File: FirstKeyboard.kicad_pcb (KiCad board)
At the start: 2 copper layers, 32 parts, among them SW1 SW_Push, U1 ATmega32U4-AU, Y1 16MHz

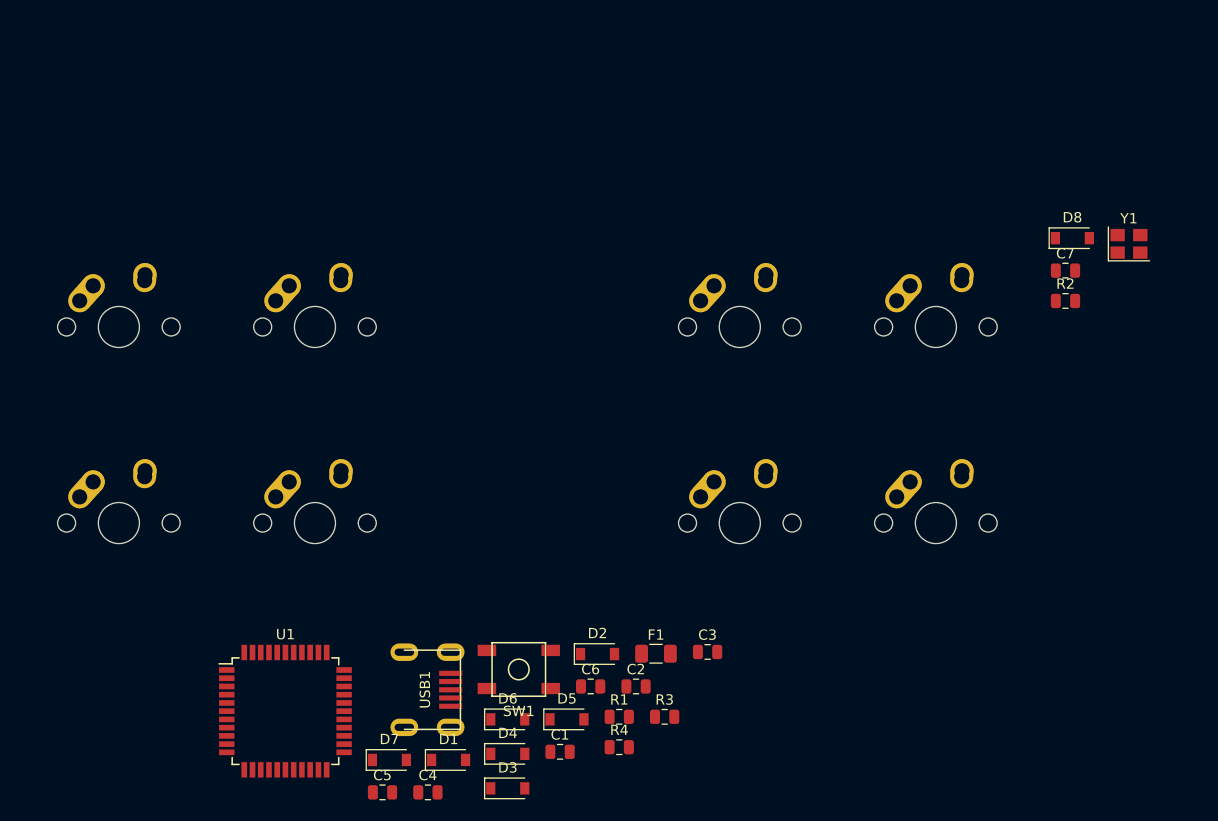
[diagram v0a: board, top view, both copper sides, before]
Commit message: Readjusted switch footprints to desired spacing of later project. Moved diodes on bottom side, within switch footprint area.
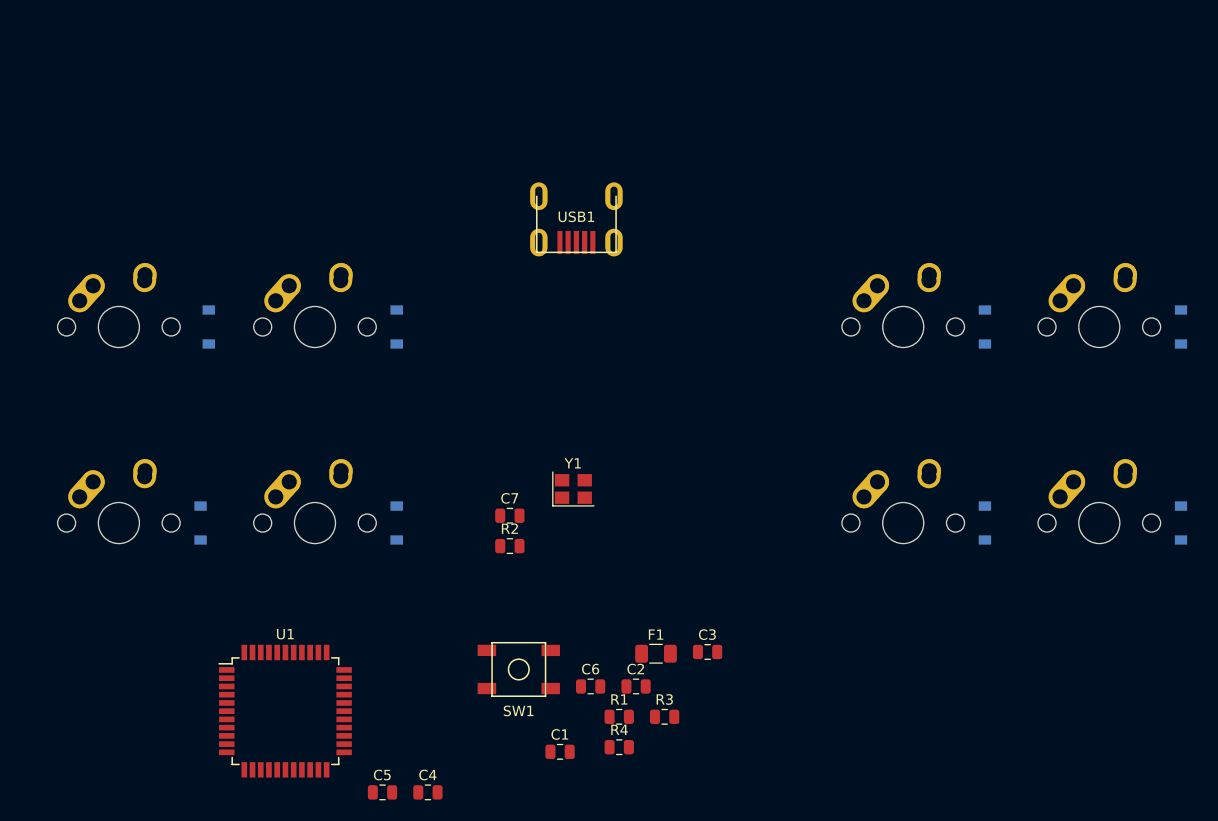
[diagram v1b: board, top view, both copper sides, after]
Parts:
- D1, D2, D3, D4, D5, D6, D7, D8: moved to B.Cu
- moved D7 87.7 mm to (209.6, 77.8), turned to 90 degrees
- moved C7 59.0 mm to (144.3, 96.1)
- moved R2 59.0 mm to (144.3, 99.1)
- moved Y1 59.0 mm to (150.5, 93.5)
- moved D5 55.7 mm to (190.5, 77.8), turned to 90 degrees
- moved USB1 50.8 mm to (150.8, 65.1), turned to 270 degrees
- moved D6 50.1 mm to (190.5, 96.8), turned to 90 degrees
- moved D1 48.1 mm to (115.1, 77.8), turned to 90 degrees
- moved D3 46.1 mm to (133.3, 77.8), turned to 90 degrees
- moved D2 40.6 mm to (114.3, 96.8), turned to 90 degrees
- moved D8 29.6 mm to (209.6, 96.8), turned to 90 degrees
- moved D4 24.9 mm to (133.3, 96.8), turned to 90 degrees
- moved MX5 15.9 mm to (182.6, 77.8)
- moved MX6 15.9 mm to (182.6, 96.8)
- moved MX7 15.9 mm to (201.6, 77.8)
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
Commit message: oops, caps are labeled differently than tutorial. Gotta figure that out later.
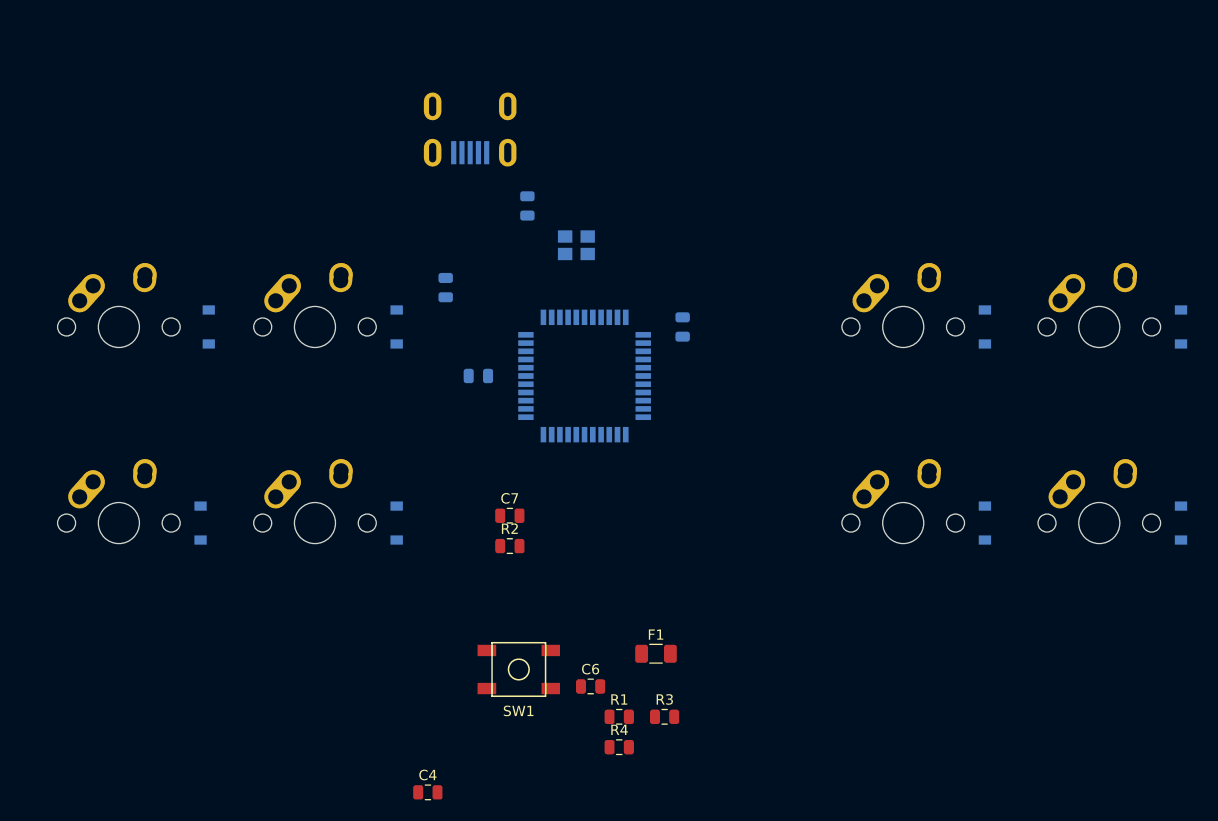
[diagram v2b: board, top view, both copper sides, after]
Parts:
- C1, C2, C3, C5, U1, USB1, Y1: moved to B.Cu
- moved C5 58.7 mm to (146.1, 66.0), turned to 90 degrees
- moved C1 46.4 mm to (138.1, 74.0), turned to 90 degrees
- moved U1 43.6 mm to (151.6, 82.5)
- moved C2 35.2 mm to (161.1, 77.8), turned to 90 degrees
- moved C3 34.9 mm to (141.3, 82.5), turned to 180 degrees
- moved Y1 23.7 mm to (150.8, 69.8), turned to 180 degrees
- moved USB1 13.5 mm to (140.5, 56.4)

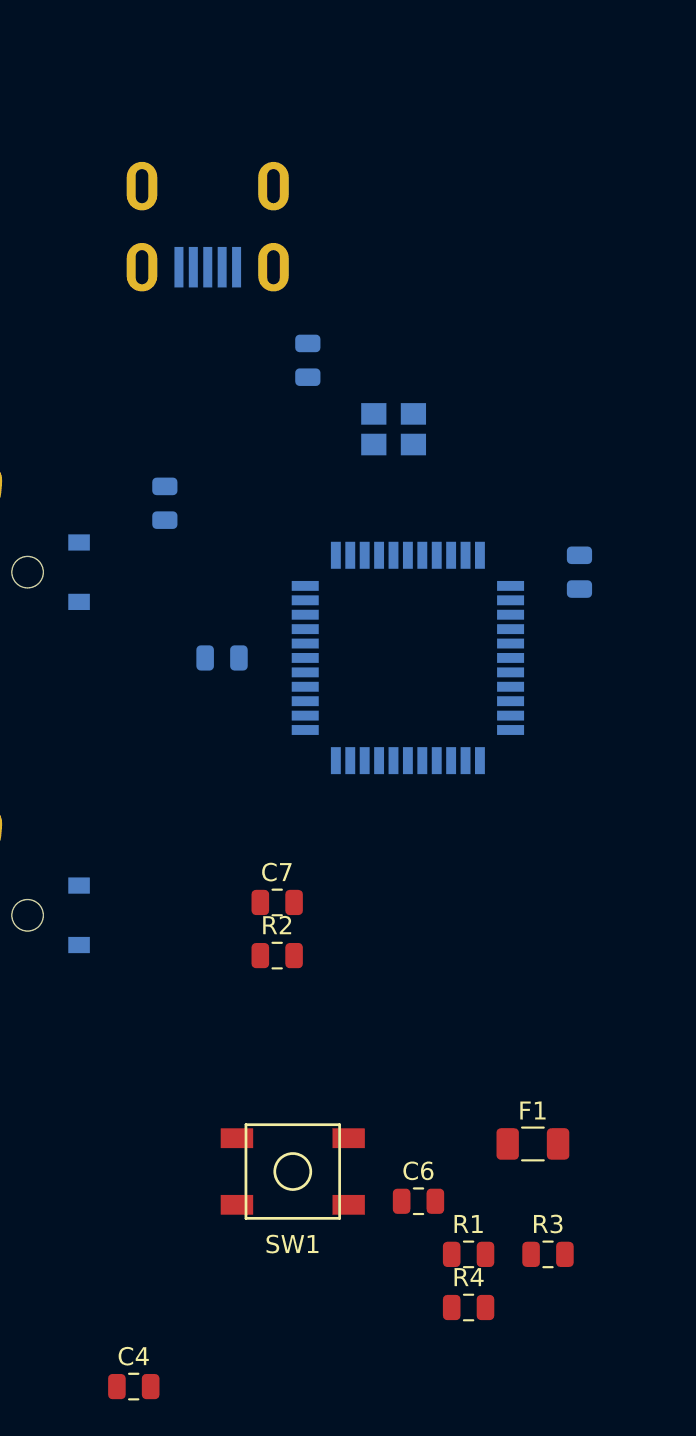
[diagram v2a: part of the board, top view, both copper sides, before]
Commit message: components should all be placed roughly appropriately, relative to each other. Will add holes for usb handwire later.
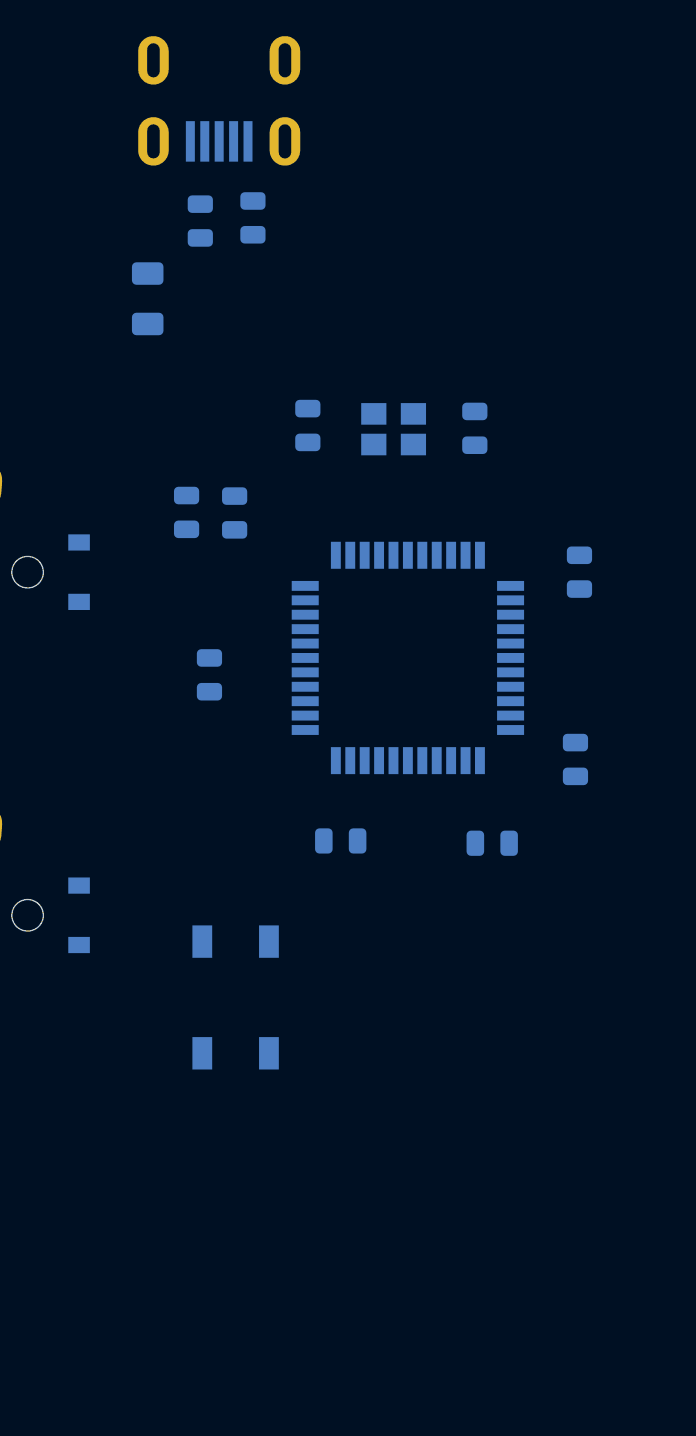
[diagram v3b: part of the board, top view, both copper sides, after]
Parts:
- C4, C6, C7, F1, R1, R2, R3, R4, SW1: moved to B.Cu
- moved R1 58.8 mm to (143.0, 58.1), turned to 90 degrees
- moved C4 54.2 mm to (146.1, 69.6), turned to 270 degrees
- moved F1 51.6 mm to (137.2, 62.6), turned to 90 degrees
- moved R3 45.8 mm to (139.3, 74.5), turned to 90 degrees
- moved C6 43.0 mm to (155.3, 69.8), turned to 90 degrees
- moved R2 41.0 mm to (140.1, 58.3), turned to 90 degrees
- moved R4 31.0 mm to (160.9, 88.2), turned to 90 degrees
- moved C5 26.7 mm to (147.9, 92.7), turned to 0 degrees
- moved C3 18.2 mm to (156.3, 92.8)
- moved C7 13.2 mm to (140.6, 83.5), turned to 270 degrees
- moved SW1 10.2 mm to (142.0, 101.4), turned to 270 degrees
- moved USB1 7.01 mm to (141.1, 49.4)
- moved C1 3.91 mm to (142.0, 74.5)
